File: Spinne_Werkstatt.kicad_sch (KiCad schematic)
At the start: 20 parts, among them J1 Conn_01x02_Pin, J3 Conn_01x03_Pin, Q1 BSS138, Q2 BSS138, U1 ESP32-WROOM-32UE, U2 CH340C

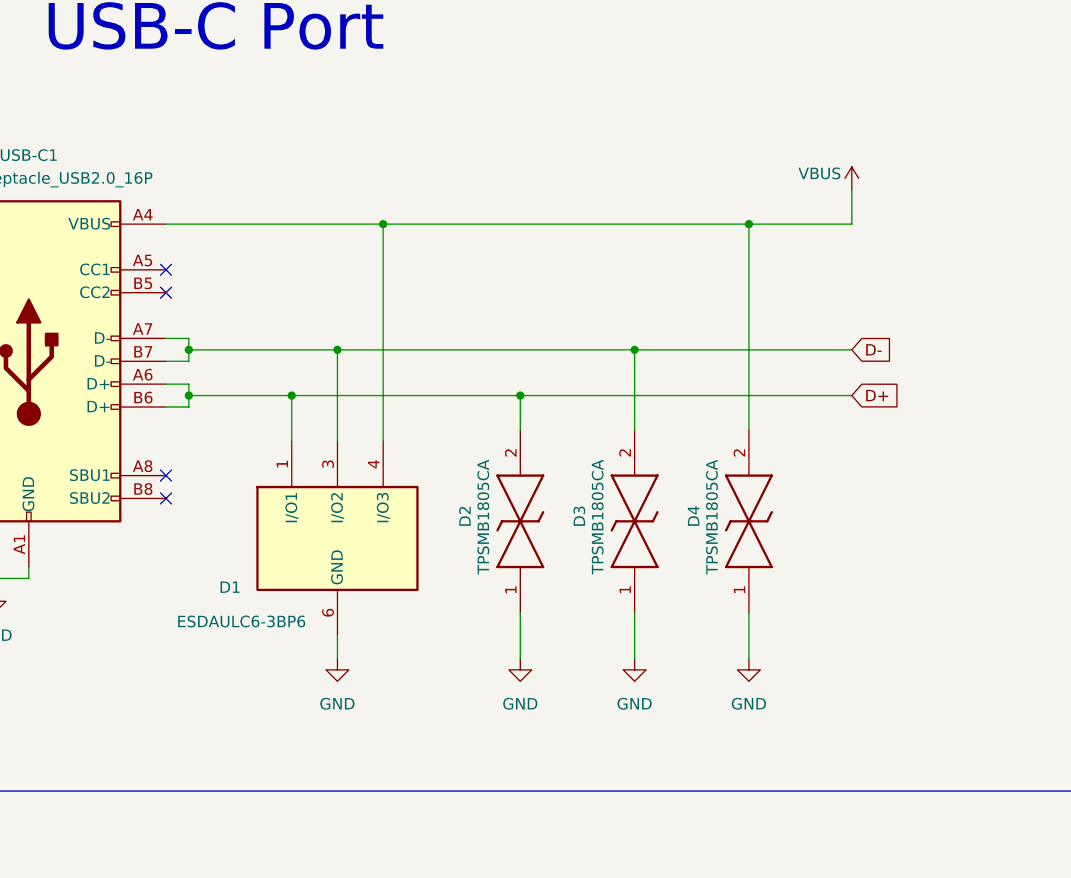
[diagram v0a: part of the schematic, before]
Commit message: removed usb data protection ic, improvements -- version 1.1.4
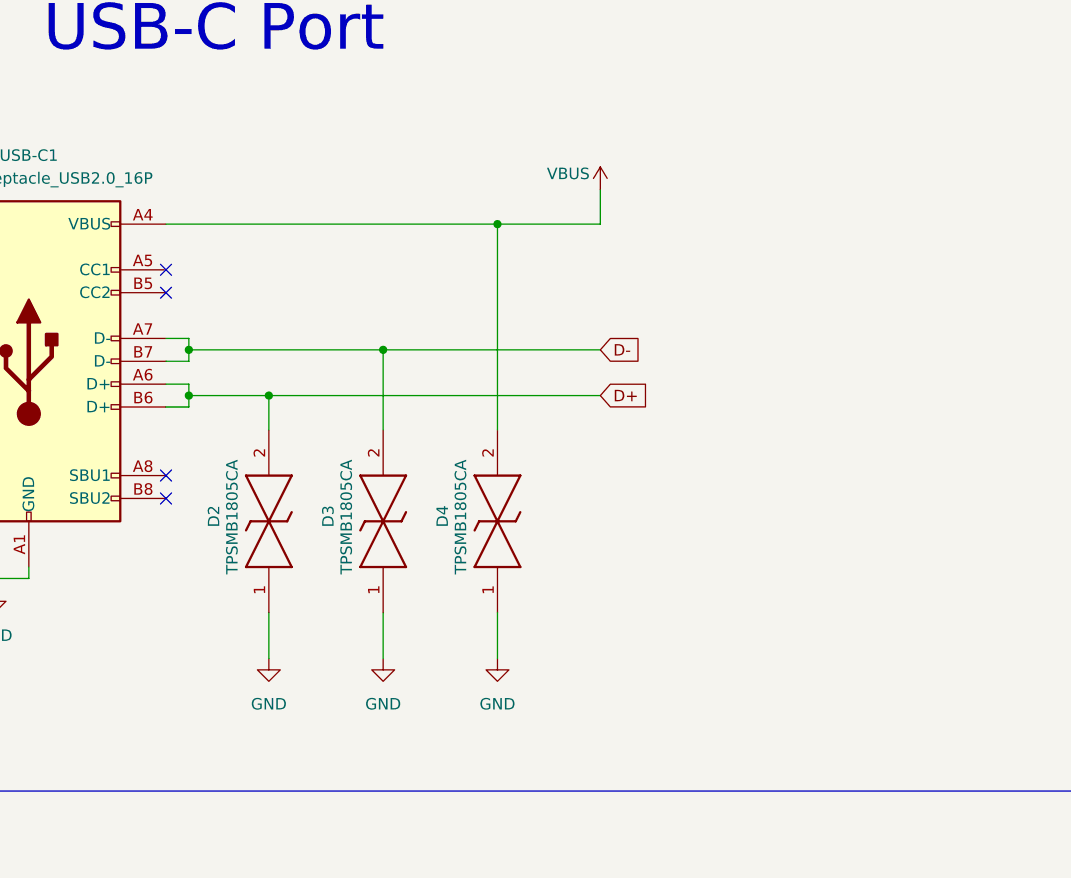
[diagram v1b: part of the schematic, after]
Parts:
- removed D1: ESDAULC6-3BP6, bulme_footprints:ESDAULC63BP6, symbol bulme_schematics:ESDAULC6-3BP6
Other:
- moved on the sheet: D2, D3, D4

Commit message: test
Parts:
- added BOOT, RST: SW_Push, Button_Switch_THT:SW_PUSH_6mm_H5mm, symbol Switch:SW_Push
- added C_BOOT, C_RST: 100nF, Capacitor_SMD:C_0805_2012Metric_Pad1.18x1.45mm_HandSolder, symbol Device:C
- added D_Onboard, D_Status: RED, Diode_SMD:D_1206_3216Metric_Pad1.42x1.75mm_HandSolder, symbol Device:LED
- added EN_PU: 10k, Resistor_SMD:R_0805_2012Metric_Pad1.20x1.40mm_HandSolder, symbol Device:R
- added R_D_Onboard, R_D_Status: 80, Resistor_SMD:R_0805_2012Metric_Pad1.20x1.40mm_HandSolder, symbol Device:R
- C_3.3V1, C_5V1: value 1uF -> 10uF
- ESP_EN_R1: footprint Resistor_SMD:R_1206_3216Metric_Pad1.30x1.75mm_HandSolder -> Resistor_SMD:R_0805_2012Metric_Pad1.20x1.40mm_HandSolder
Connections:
- net +3V3: now also EN_PU.1, R_D_Onboard.1, R_D_Status.1
- net ESP32_IO0: now also BOOT.2, C_BOOT.1
- net GND: now also BOOT.1, C_BOOT.2, C_RST.2, D_Status.1 (K), RST.1
- net pin30: now also D_Onboard.1 (K)
- new net: D_Status.2 (A), R_D_Status.2
- new net: C_RST.1, EN_PU.2, RST.2
- new net: D_Onboard.2 (A), R_D_Onboard.2
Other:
- note added: "BUTTON"
- note added: "LEDs"
- note removed: "10uF auf oshw"
- note removed: "NIMM 10uF"
- moved on the sheet: AMS1117, C_3.3V1, C_5V1, C_ESP1, C_ESP2, D2, D3, D4, J1, J3, U1, USB-C1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
